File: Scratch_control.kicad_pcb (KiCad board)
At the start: 2 copper layers, 61 x 61.7 mm, 40 parts, among them J1 OUTPUT1, J2 OUTPUT2, J3 OUTPUT3, J4 Conn_01x02, J5 Conn_01x04, K1 Key, K2 Key, K3 Key, K4 Key, U1 AMS1117-3.3, U2 TPS54540, U3 STM32G030F6Px, X1 8M

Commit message: Update whole project.Delete some useless pin and so on....
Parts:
- removed X1: 8M, Crystal:Crystal_HC49-U_Vertical
- added R11: 10k, Resistor_SMD:R_0603_1608Metric, F.Cu at (139.7, 128.3)
- added RST1: Key, Button_Switch_SMD:SW_DIP_SPSTx01_Slide_6.7x4.1mm_W6.73mm_P2.54mm_LowProfile_JPin, F.Cu at (132.7, 135.9)
- C11: value 47uF -> 100nF; footprint Capacitor_SMD:C_0805_2012Metric -> Capacitor_SMD:C_0603_1608Metric
- C12: value 22pF -> 100nF
- C13: value 22pF -> 47uF; footprint Capacitor_SMD:C_0603_1608Metric -> Capacitor_SMD:CP_Elec_8x10
- J1: value OUTPUT1 -> MG995; footprint Connector_JST:JST_GH_SM05B-GHS-TB_1x05-1MP_P1.25mm_Horizontal -> Connector_PinHeader_2.54mm:PinHeader_1x03_P2.54mm_Horizontal
- J2: value OUTPUT2 -> LED; footprint Connector_JST:JST_GH_SM05B-GHS-TB_1x05-1MP_P1.25mm_Horizontal -> Connector_PinHeader_2.54mm:PinHeader_1x03_P2.54mm_Horizontal
- J3: value OUTPUT3 -> SENSOR; footprint Connector_JST:JST_GH_SM05B-GHS-TB_1x05-1MP_P1.25mm_Horizontal -> Connector_JST:JST_GH_SM03B-GHS-TB_1x03-1MP_P1.25mm_Horizontal
- J5: moved to F.Cu
- R8: value 11.5k -> 20k
- R9: value 60.4k -> 105k
- moved C11 50.0 mm to (137.2, 128.3)
- moved C13 45.3 mm to (181.9, 120.9), turned to 0 degrees
- moved C5 41.5 mm to (184.2, 112.5)
- moved R4 37.5 mm to (150.6, 120.4), turned to 180 degrees
- moved C1 32.3 mm to (150.6, 117.6), turned to 0 degrees
- moved C4 30.0 mm to (150.6, 115.6), turned to 180 degrees
- moved R8 27.8 mm to (166.7, 120.5), turned to 180 degrees
- moved U2 26.9 mm to (158.6, 118.4), turned to 0 degrees
- moved C9 25.0 mm to (184.2, 109.9)
- moved R9 24.9 mm to (166.6, 118.5), turned to 0 degrees
- moved J3 23.9 mm to (159.5, 96.8)
- moved J2 23.2 mm to (176.4, 98.2), turned to 90 degrees
- moved D3 22.2 mm to (151.4, 109.3), turned to -90 degrees
- moved C2 22.1 mm to (166.6, 116.5), turned to 0 degrees
- moved R2 19.2 mm to (166.6, 114.4), turned to 0 degrees
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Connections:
- C11 pad 2: +24V -> /KEY4
- C12 pad 2: Net-(C12-Pad2) -> +3V3
- C13 pad 1: GND -> +24V
- C13 pad 2: Net-(C13-Pad2) -> GND
- J1 pad 1: +5V -> /PWM4
- J1 pad 2: GND -> +5V
- J1 pad 3: /PWM2 -> GND
- J2 pad 2: GND -> /PWM3
- J2 pad 3: /PWM4 -> GND
- J3 pad 1: +5V -> GND
- J3 pad 2: GND -> /SENSOR
- J3 pad 3: /PWM6 -> +5V
- J5 pad 1: +3V3 -> GND
- J5 pad 2: /SWDIO -> /SWCLK
- J5 pad 3: /SWCLK -> /SWDIO
- J5 pad 4: GND -> +3V3
- K4 pad 1: Net-(C10-Pad2) -> /KEY4
- U3 pad 1: /SENSOR3 -> unconnected-(U3-Pad1)
- U3 pad 10: /SENSOR2 -> /KEY4
- U3 pad 11: /PWM1 -> unconnected-(U3-Pad11)
- U3 pad 12: /KEY3 -> unconnected-(U3-Pad12)
- U3 pad 13: /PWM2 -> /SENSOR
- U3 pad 16: /PWM5 -> unconnected-(U3-Pad16)
- U3 pad 2: Net-(C12-Pad2) -> unconnected-(U3-Pad2)
- U3 pad 20: /PWM6 -> unconnected-(U3-Pad20)
- U3 pad 3: Net-(C13-Pad2) -> unconnected-(U3-Pad3)
- U3 pad 9: /SENSOR1 -> /KEY3
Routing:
- net /SENSOR2: track 75.6 -> 0.00 mm
- net /SENSOR1: track 47.8 -> 0.00 mm
- net /PWM5: track 44.4 -> 0.00 mm
- net /SENSOR3: track 41.8 -> 0.00 mm, vias 2 -> 0
- net /PWM6: track 41.4 -> 0.00 mm
- net /SENSOR: track 0.00 -> 40.4 mm, vias 0 -> 2
- net GND: track 45.3 -> 6.39 mm, vias 31 -> 104
- net /PWM1: track 33.4 -> 0.00 mm
- net /PWM2: track 31.6 -> 0.00 mm
- net /PWM3: track 25.6 -> 55.6 mm, vias 0 -> 2
- net +24V: track 31.6 -> 58.1 mm
- net +3V3: track 136.0 -> 159.9 mm, vias 5 -> 7
- net /LED1: track 22.7 -> 43.9 mm
- net /KEY4: track 0.00 -> 19.4 mm
- net Net-(C13-Pad2): track 17.9 -> 0.00 mm
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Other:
- board size 61 x 61.7 mm -> 61 x 49 mm
- board text added: "+5V"
- board text added: "CLK"
- board text added: "DIO"
- board text added: "GND"
- board text added: "LED"
- board text added: "LED1"
- board text added: "MG995"
- board text added: "PWM"
- board text added: "PWR"
- board text added: "SENSOR"
- board text added: "VCC"

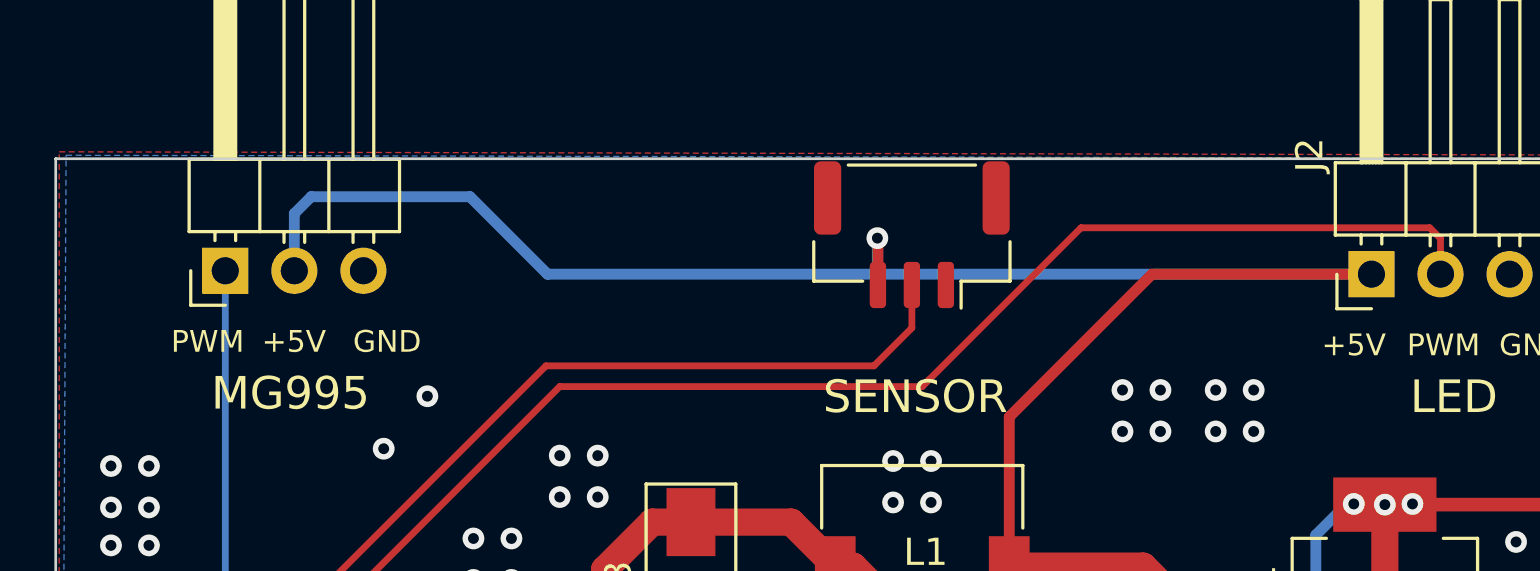
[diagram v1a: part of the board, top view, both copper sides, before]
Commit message: add some decoupling capacitors
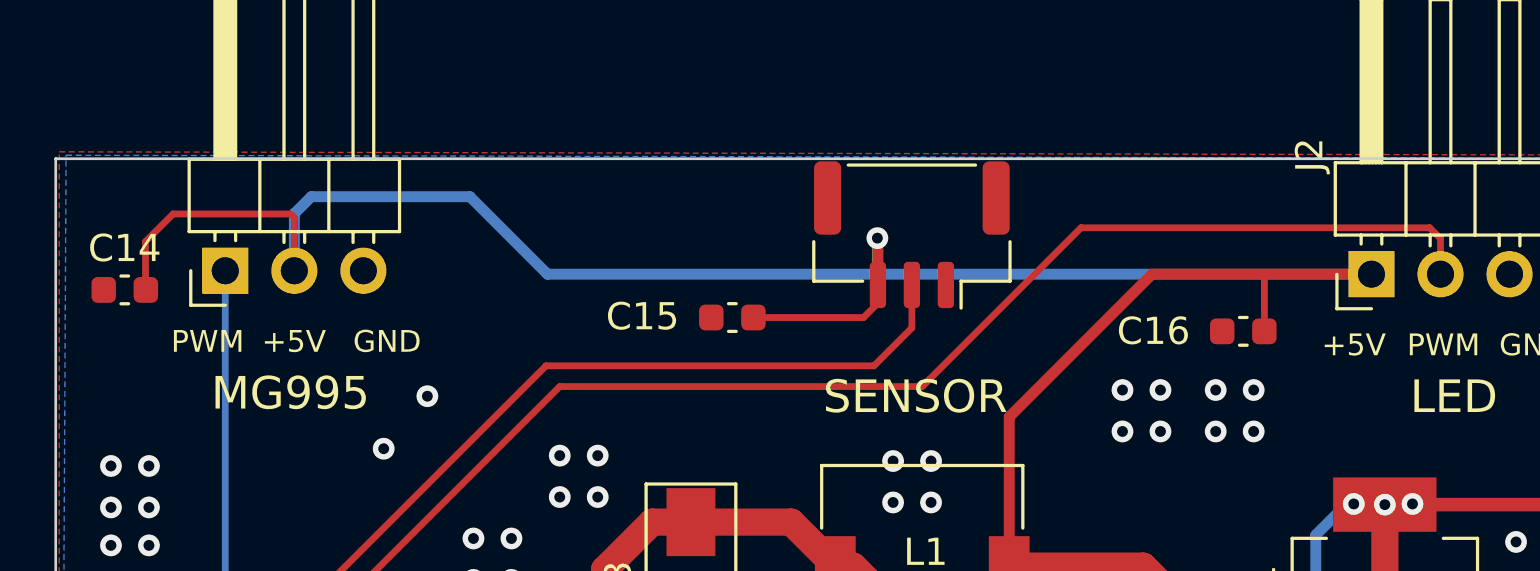
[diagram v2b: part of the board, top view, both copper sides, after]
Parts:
- added C14: 47uF, Capacitor_SMD:C_0603_1608Metric, F.Cu at (130.6, 98.8)
- added C15: 47uF, Capacitor_SMD:C_0603_1608Metric, F.Cu at (152.9, 99.8)
- added C16: 47uF, Capacitor_SMD:C_0603_1608Metric, F.Cu at (171.7, 100.3)
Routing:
- net +5V: track 104.0 -> 121.3 mm
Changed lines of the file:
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@@
       (drillshape 0)
       (scaleselection 1)
-      (outputdirectory "")
+      (outputdirectory "pcb_output/")
     )
   )
@@
       (net 2 "+24V") (pintype "passive"))
     (model "${KICAD6_3DMODEL_DIR}/Capacitor_SMD.3dshapes/C_0805_2012Metric.wrl"
+      (offset (xyz 0 0 0))
+      (scale (xyz 1 1 1))
+      (rotate (xyz 0 0 0))
+    )
+  )
+  (footprint "Capacitor_SMD:C_0603_1608Metric" (layer "F.Cu")
+    (at 152.908 99.822)
+    (descr "Capacitor SMD 0603 (1608 Metric), square (rectangular) end terminal, IPC_7351 nominal, (Body size source: IPC-SM-782 page 76, https://www.pcb-3d.com/wordpress/wp-content/uploads/ipc-sm-782a_amendment_1_and_2.pdf), generated with kicad-footprint-generator")
+    (tags "capacitor")
+    (property "Sheetfile" "Scratch_control.kicad_sch")
+    (property "Sheetname" "")
+    (attr smd)
+    (fp_text reference "C15" (at -3.302 -0.03) (layer "F.SilkS")
+      (effects (font (size 1 1) (thickness 0.15)))
+    )
+    (fp_text value "47uF" (at 0 1.43) (layer "F.Fab")
+      (effects (font (size 1 1) (thickness 0.15)))
+    )
+    (fp_text user "${REFERENCE}" (at 0 0) (layer "F.Fab")
+      (effects (font (size 0.4 0.4) (thickness 0.06)))
+    )
+    (fp_line (start -0.14058 0.51) (end 0.14058 0.51) (layer "F.SilkS") (width 0.12))
+    (fp_line (start -0.14058 -0.51) (end 0.14058 -0.51) (layer "F.SilkS") (width 0.12))
+    (fp_line (start 1.48 0.73) (end -1.48 0.73) (layer "F.CrtYd") (width 0.05))
+    (fp_line (start 1.48 -0.73) (end 1.48 0.73) (layer "F.CrtYd") (width 0.05))
+    (fp_line (start -1.48 -0.73) (end 1.48 -0.73) (layer "F.CrtYd") (width 0.05))
+    (fp_line (start -1.48 0.73) (end -1.48 -0.73) (layer "F.CrtYd") (width 0.05))
+    (fp_line (start 0.8 0.4) (end -0.8 0.4) (layer "F.Fab") (width 0.1))
+    (fp_line (start -0.8 -0.4) (end 0.8 -0.4) (layer "F.Fab") (width 0.1))
+    (fp_line (start 0.8 -0.4) (end 0.8 0.4) (layer "F.Fab") (width 0.1))
+    (fp_line (start -0.8 0.4) (end -0.8 -0.4) (layer "F.Fab") (width 0.1))
+    (pad "1" smd roundrect (at -0.775 0) (size 0.9 0.95) (layers "F.Cu" "F.Paste" "F.Mask") (roundrect_rratio 0.25)
+      (net 1 "GND") (pintype "passive"))
+    (pad "2" smd roundrect (at 0.775 0) (size 0.9 0.95) (layers "F.Cu" "F.Paste" "F.Mask") (roundrect_rratio 0.25)
+      (net 11 "+5V") (pintype "passive"))
+    (model "${KICAD6_3DMODEL_DIR}/Capacitor_SMD.3dshapes/C_0603_1608Metric.wrl"
       (offset (xyz 0 0 0))
       (scale (xyz 1 1 1))
@@
     )
   )
+  (footprint "Capacitor_SMD:C_0603_1608Metric" (layer "F.Cu")
+    (at 130.556 98.806)
+    (descr "Capacitor SMD 0603 (1608 Metric), square (rectangular) end terminal, IPC_7351 nominal, (Body size source: IPC-SM-782 page 76, https://www.pcb-3d.com/wordpress/wp-content/uploads/ipc-sm-782a_amendment_1_and_2.pdf), generated with kicad-footprint-generator")
+    (tags "capacitor")
+    (property "Sheetfile" "Scratch_control.kicad_sch")
+    (property "Sheetname" "")
+    (attr smd)
+    (fp_text reference "C14" (at 0 -1.524) (layer "F.SilkS")
+      (effects (font (size 1 1) (thickness 0.15)))
+    )
+    (fp_text value "47uF" (at 0 1.43) (layer "F.Fab")
+      (effects (font (size 1 1) (thickness 0.15)))
+    )
+    (fp_text user "${REFERENCE}" (at 0 0) (layer "F.Fab")
+      (effects (font (size 0.4 0.4) (thickness 0.06)))
+    )
+    (fp_line (start -0.14058 0.51) (end 0.14058 0.51) (layer "F.SilkS") (width 0.12))
+    (fp_line (start -0.14058 -0.51) (end 0.14058 -0.51) (layer "F.SilkS") (width 0.12))
+    (fp_line (start -1.48 0.73) (end -1.48 -0.73) (layer "F.CrtYd") (width 0.05))
+    (fp_line (start 1.48 -0.73) (end 1.48 0.73) (layer "F.CrtYd") (width 0.05))
+    (fp_line (start -1.48 -0.73) (end 1.48 -0.73) (layer "F.CrtYd") (width 0.05))
+    (fp_line (start 1.48 0.73) (end -1.48 0.73) (layer "F.CrtYd") (width 0.05))
+    (fp_line (start 0.8 0.4) (end -0.8 0.4) (layer "F.Fab") (width 0.1))
+    (fp_line (start 0.8 -0.4) (end 0.8 0.4) (layer "F.Fab") (width 0.1))
+    (fp_line (start -0.8 0.4) (end -0.8 -0.4) (layer "F.Fab") (width 0.1))
+    (fp_line (start -0.8 -0.4) (end 0.8 -0.4) (layer "F.Fab") (width 0.1))
+    (pad "1" smd roundrect (at -0.775 0) (size 0.9 0.95) (layers "F.Cu" "F.Paste" "F.Mask") (roundrect_rratio 0.25)
+      (net 1 "GND") (pintype "passive"))
+    (pad "2" smd roundrect (at 0.775 0) (size 0.9 0.95) (layers "F.Cu" "F.Paste" "F.Mask") (roundrect_rratio 0.25)
+      (net 11 "+5V") (pintype "passive"))
+    (model "${KICAD6_3DMODEL_DIR}/Capacitor_SMD.3dshapes/C_0603_1608Metric.wrl"
+      (offset (xyz 0 0 0))
+      (scale (xyz 1 1 1))
+      (rotate (xyz 0 0 0))
+    )
+  )
   (footprint "Resistor_SMD:R_0603_1608Metric" (layer "F.Cu")
     (at 166.624 114.427)
@@
       (net 9 "/KEY2") (pintype "passive"))
     (model "${KICAD6_3DMODEL_DIR}/Resistor_SMD.3dshapes/R_0603_1608Metric.wrl"
+      (offset (xyz 0 0 0))
+      (scale (xyz 1 1 1))
+      (rotate (xyz 0 0 0))
+    )
+  )
+  (footprint "Capacitor_SMD:C_0603_1608Metric" (layer "F.Cu")
+    (at 171.704 100.33)
+    (descr "Capacitor SMD 0603 (1608 Metric), square (rectangular) end terminal, IPC_7351 nominal, (Body size source: IPC-SM-782 page 76, https://www.pcb-3d.com/wordpress/wp-content/uploads/ipc-sm-782a_amendment_1_and_2.pdf), generated with kicad-footprint-generator")
+    (tags "capacitor")
+    (property "Sheetfile" "Scratch_control.kicad_sch")
+    (property "Sheetname" "")
+    (attr smd)
+    (fp_text reference "C16" (at -3.302 0) (layer "F.SilkS")
+      (effects (font (size 1 1) (thickness 0.15)))
+    )
+    (fp_text value "47uF" (at 0 1.43) (layer "F.Fab")
+      (effects (font (size 1 1) (thickness 0.15)))
+    )
+    (fp_text user "${REFERENCE}" (at 0 0) (layer "F.Fab")
+      (effects (font (size 0.4 0.4) (thickness 0.06)))
+    )
+    (fp_line (start -0.14058 0.51) (end 0.14058 0.51) (layer "F.SilkS") (width 0.12))
+    (fp_line (start -0.14058 -0.51) (end 0.14058 -0.51) (layer "F.SilkS") (width 0.12))
+    (fp_line (start -1.48 -0.73) (end 1.48 -0.73) (layer "F.CrtYd") (width 0.05))
+    (fp_line (start -1.48 0.73) (end -1.48 -0.73) (layer "F.CrtYd") (width 0.05))
+    (fp_line (start 1.48 -0.73) (end 1.48 0.73) (layer "F.CrtYd") (width 0.05))
+    (fp_line (start 1.48 0.73) (end -1.48 0.73) (layer "F.CrtYd") (width 0.05))
+    (fp_line (start -0.8 -0.4) (end 0.8 -0.4) (layer "F.Fab") (width 0.1))
+    (fp_line (start 0.8 0.4) (end -0.8 0.4) (layer "F.Fab") (width 0.1))
+    (fp_line (start -0.8 0.4) (end -0.8 -0.4) (layer "F.Fab") (width 0.1))
+    (fp_line (start 0.8 -0.4) (end 0.8 0.4) (layer "F.Fab") (width 0.1))
+    (pad "1" smd roundrect (at -0.775 0) (size 0.9 0.95) (layers "F.Cu" "F.Paste" "F.Mask") (roundrect_rratio 0.25)
+      (net 1 "GND") (pintype "passive"))
+    (pad "2" smd roundrect (at 0.775 0) (size 0.9 0.95) (layers "F.Cu" "F.Paste" "F.Mask") (roundrect_rratio 0.25)
+      (net 11 "+5V") (pintype "passive"))
+    (model "${KICAD6_3DMODEL_DIR}/Capacitor_SMD.3dshapes/C_0603_1608Metric.wrl"
       (offset (xyz 0 0 0))
       (scale (xyz 1 1 1))
@@
   (segment (start 143.51 127.382) (end 144.514 127.382) (width 0.2) (layer "F.Cu") (net 10))
   (segment (start 146.177 130.429) (end 146.177 129.045) (width 0.2) (layer "F.Cu") (net 10))
+  (segment (start 131.331 98.806) (end 131.318 98.793) (width 0.25) (layer "F.Cu") (net 11))
   (segment (start 179.211 115.005) (end 175.852 118.364) (width 1) (layer "F.Cu") (net 11))
+  (segment (start 153.683 99.822) (end 157.734 99.822) (width 0.25) (layer "F.Cu") (net 11))
   (segment (start 168.021 108.966) (end 163.093 108.966) (width 1) (layer "F.Cu") (net 11))
+  (segment (start 136.794 96.154) (end 136.794 98.101) (width 0.25) (layer "F.Cu") (net 11))
   (segment (start 158.262 98.624) (end 158.262 96.921) (width 0.4) (layer "F.Cu") (net 11))
   (segment (start 169.799 110.744) (end 168.021 108.966) (width 1) (layer "F.Cu") (net 11))
+  (segment (start 157.734 99.822) (end 158.262 99.294) (width 0.25) (layer "F.Cu") (net 11))
+  (segment (start 168.345 98.228) (end 172.396 98.228) (width 0.4) (layer "F.Cu") (net 11))
+  (segment (start 172.479 100.33) (end 172.479 98.311) (width 0.25) (layer "F.Cu") (net 11))
   (segment (start 158.262 96.921) (end 158.242 96.901) (width 0.4) (layer "F.Cu") (net 11))
+  (segment (start 131.318 98.793) (end 131.318 97.028) (width 0.25) (layer "F.Cu") (net 11))
   (segment (start 170.688 118.364) (end 169.799 117.475) (width 1) (layer "F.Cu") (net 11))
   (segment (start 179.211 113.005) (end 179.211 110.984) (width 1) (layer "F.Cu") (net 11))
   (segment (start 175.852 118.364) (end 170.688 118.364) (width 1) (layer "F.Cu") (net 11))
   (segment (start 163.093 108.966) (end 163.093 103.48) (width 0.4) (layer "F.Cu") (net 11))
+  (segment (start 158.262 99.294) (end 158.262 98.624) (width 0.25) (layer "F.Cu") (net 11))
   (segment (start 179.211 110.984) (end 180.34 109.855) (width 1) (layer "F.Cu") (net 11))
-  (segment (start 168.345 98.228) (end 176.418 98.228) (width 0.4) (layer "F.Cu") (net 11))
   (segment (start 167.449 118.491) (end 168.783 118.491) (width 0.2) (layer "F.Cu") (net 11))
+  (segment (start 132.334 96.012) (end 136.652 96.012) (width 0.25) (layer "F.Cu") (net 11))
+  (segment (start 172.479 98.311) (end 172.396 98.228) (width 0.25) (layer "F.Cu") (net 11))
   (segment (start 180.34 109.855) (end 183.375 109.855) (width 1) (layer "F.Cu") (net 11))
+  (segment (start 131.318 97.028) (end 132.334 96.012) (width 0.25) (layer "F.Cu") (net 11))
   (segment (start 168.783 118.491) (end 169.799 117.475) (width 0.2) (layer "F.Cu") (net 11))
+  (segment (start 136.652 96.012) (end 136.794 96.154) (width 0.25) (layer "F.Cu") (net 11))
+  (segment (start 172.396 98.228) (end 176.418 98.228) (width 0.4) (layer "F.Cu") (net 11))
   (segment (start 169.799 117.475) (end 169.799 110.744) (width 1) (layer "F.Cu") (net 11))
   (segment (start 163.093 103.48) (end 168.345 98.228) (width 0.4) (layer "F.Cu") (net 11))
